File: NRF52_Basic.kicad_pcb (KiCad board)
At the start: 4 copper layers, 18.2 x 19.2 mm, 18 parts, among them J1 Conn_01x05_Male, J2 Conn_01x05_Male, J3 Conn_01x04_Male, J4 Conn_Coaxial, U1 nRF52832-QFxx, Y1 Crystal, Y2 Crystal

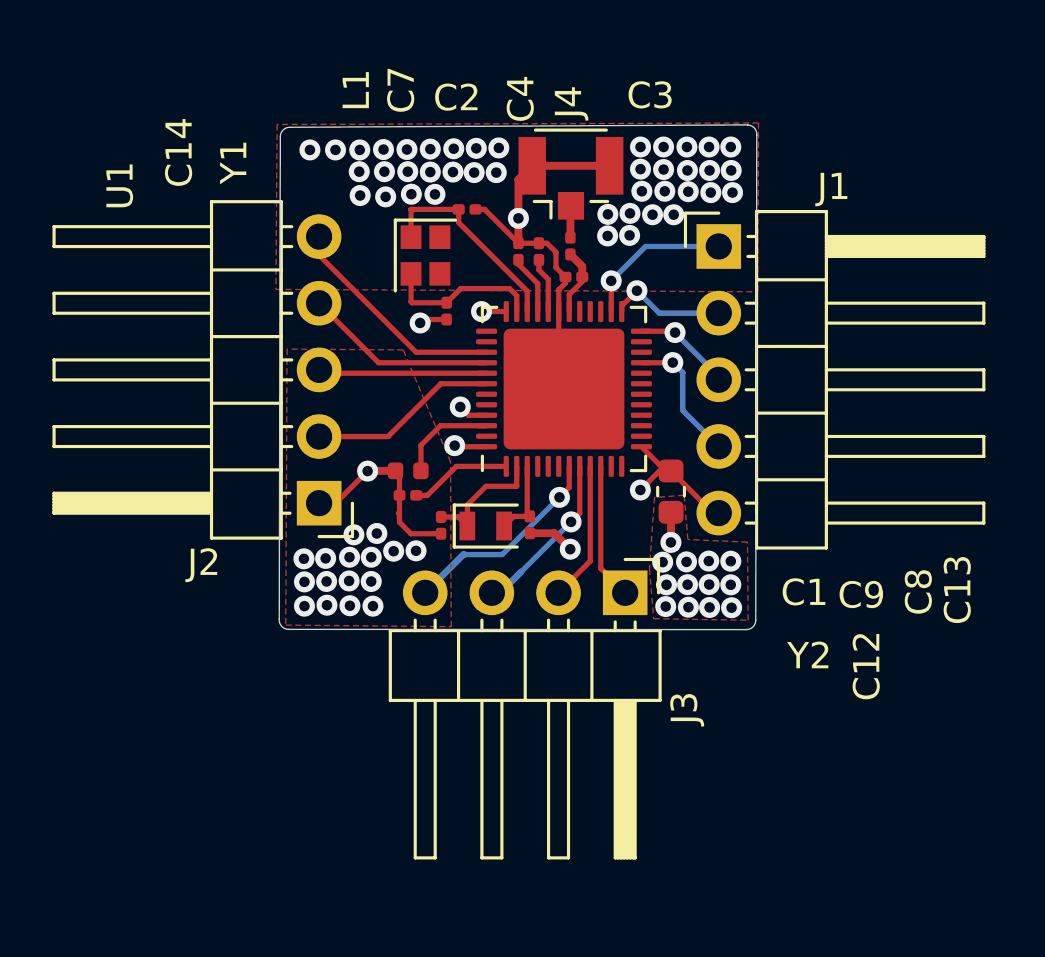
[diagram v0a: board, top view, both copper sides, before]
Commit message: Improved ground fills and structure
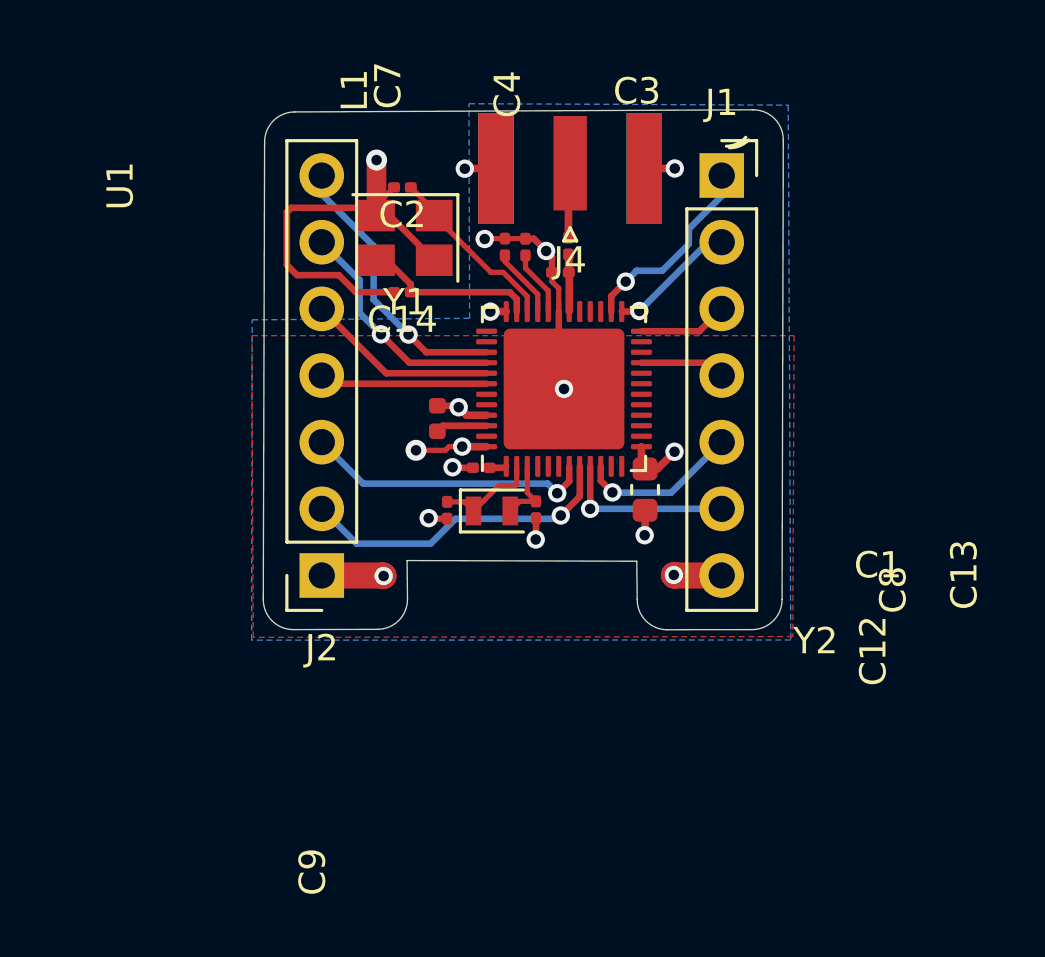
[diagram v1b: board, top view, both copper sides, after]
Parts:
- removed J3: Conn_01x04_Male, Connector_PinHeader_2.54mm:PinHeader_1x04_P2.54mm_Horizontal
- J1, J2: value Conn_01x05_Male -> Conn_01x07_Male; footprint Connector_PinHeader_2.54mm:PinHeader_1x05_P2.54mm_Horizontal -> Connector_PinSocket_2.54mm:PinSocket_1x07_P2.54mm_Vertical
- J4: footprint Connector_Coaxial:U.FL_Hirose_U.FL-R-SMT-1_Vertical -> Connector_Coaxial:SMA_Samtec_SMA-J-P-H-ST-EM1_EdgeMount
- Y1: value Crystal -> Crystal_GND24; footprint Crystal:Crystal_SMD_2016-4Pin_2.0x1.6mm -> Crystal:Crystal_SMD_3225-4Pin_3.2x2.5mm
- moved C1 2.99 mm to (143.2, 86.4)
- moved J2 2.76 mm to (137.1, 90.5)
- moved J1 2.70 mm to (152.4, 75.3)
- moved C2 2.60 mm to (140.2, 75.7), turned to 180 degrees
- moved C9 2.28 mm to (141.5, 84.5), turned to 270 degrees
- moved C14 1.83 mm to (140.2, 79.7), turned to 180 degrees
- moved Y1 1.02 mm to (140.3, 77.7), turned to 180 degrees
- moved C8 0.99 mm to (149.5, 87.3)
- moved C13 0.62 mm to (145.3, 88.0)
- moved C12 0.62 mm to (141.9, 88.0)
- moved Y2 0.62 mm to (143.6, 88.1)
- moved C3 0.54 mm to (146.2, 79.0)
- moved C4 0.54 mm to (144.9, 78.0)
- moved C7 0.54 mm to (144.1, 78.0)
- moved J4 0.37 mm to (146.6, 75.0)
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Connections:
- J1 pad 5: VDD -> 0.08_RX
- J2 pad 2: 0.30 -> 0.06_TX
- J2 pad 3: 0.29 -> 0.05_RTS
- J2 pad 4: 0.28 -> 0.30
- J2 pad 5: 0.27 -> 0.29
- Y1 pad 2: XC2 -> VSS
- Y1 pad 3: (no net) -> XC2
- Y1 pad 4: (no net) -> VSS
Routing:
- net VSS: track 27.8 -> 34.7 mm, vias 75 -> 12
- net 0.06_TX: track 7.46 -> 12.3 mm
- net D1: track 3.89 -> 0.66 mm
- net 0.05_RTS: track 7.96 -> 11.0 mm
- net 0.27: track 8.62 -> 10.7 mm, vias 0 -> 1
- net SWO: track 5.12 -> 3.26 mm, vias 1 -> 0
- net D4: track 3.78 -> 1.96 mm
- net Net-(J4-Pad1): track 1.22 -> 2.86 mm
- net SWDIO: track 5.81 -> 7.45 mm
- net 0.28: track 7.32 -> 8.92 mm, vias 0 -> 1
- net 0.07_CTS: track 5.32 -> 6.63 mm, vias 0 -> 1
- net XC1: track 7.85 -> 6.84 mm
- net XL1: track 4.88 -> 3.89 mm
- net 0.08_RX: track 5.20 -> 6.14 mm, vias 0 -> 1
- net 0.29: track 6.43 -> 7.30 mm
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- added copper zone on B.Cu, net VDD
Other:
- board size 18.2 x 19.2 mm -> 19.8 x 19.8 mm
- net class Default: clearance 0.2 -> 0.127
- net class GND removed
- net class VCC removed
- rule trace_clearance: 0.2 -> 0.127

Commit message: Intermediate mods -2
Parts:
- C1: value C -> 100nF
- C12, C13, C14, C2: value C -> 12pF
- C3: value C -> 0.8pF
- C4, C7: value C -> 100pF
- C8: value C -> 4.7uF
- C9: value C -> 1.0uF
- L1: value L -> 3.9nH
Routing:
- net VDD: track 7.49 -> 11.5 mm, vias 5 -> 8
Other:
- board text added: "0.05/RTS"
- board text added: "0.06/TX"
- board text added: "0.07/CTS"
- board text added: "0.08/RX"
- board text added: "0.27"
- board text added: "0.28"
- board text added: "0.29"
- board text added: "0.30"
- board text added: "GND"
- board text added: "NRF52 V1 J.S.I.A"
- board text added: "RESET/0.21"
- board text added: "SWDCLK"
- board text added: "SWDIO"
- board text added: "SWO"

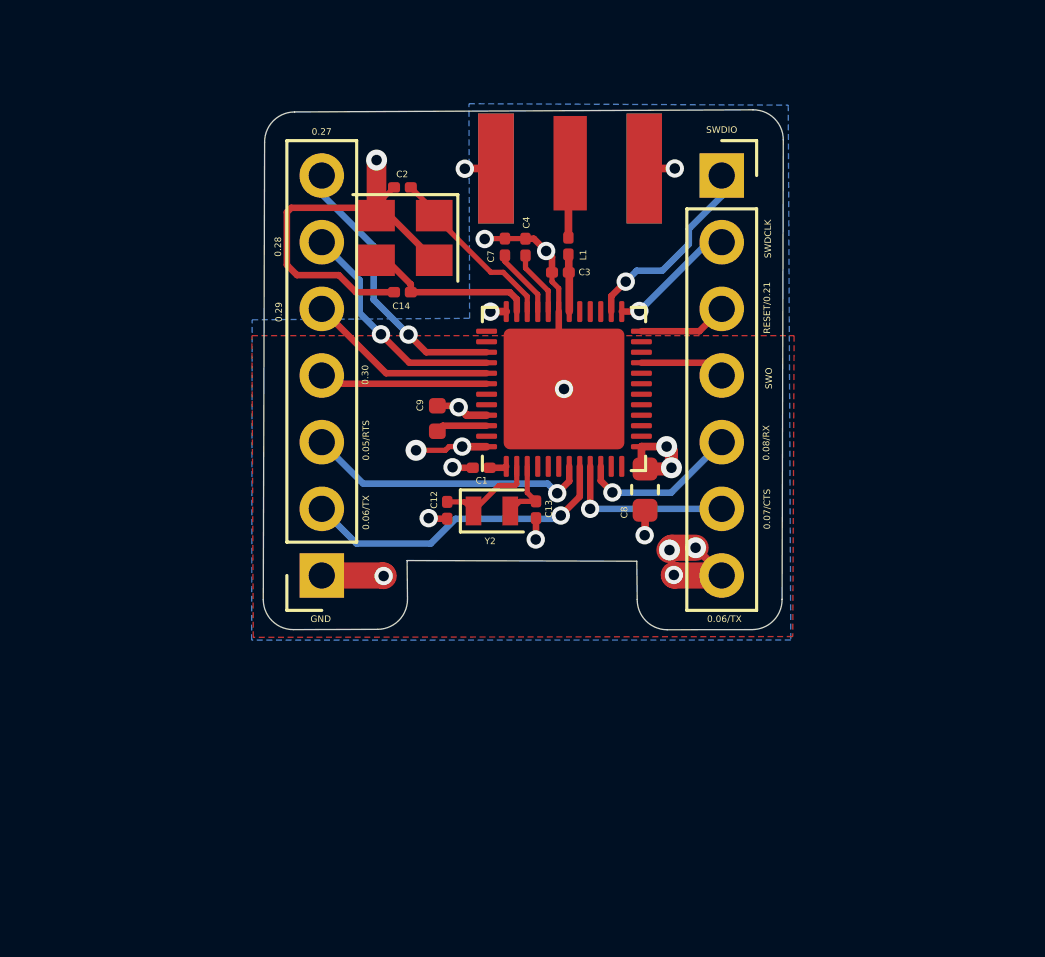
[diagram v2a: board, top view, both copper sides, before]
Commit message: Optimized the layers and component fixtures
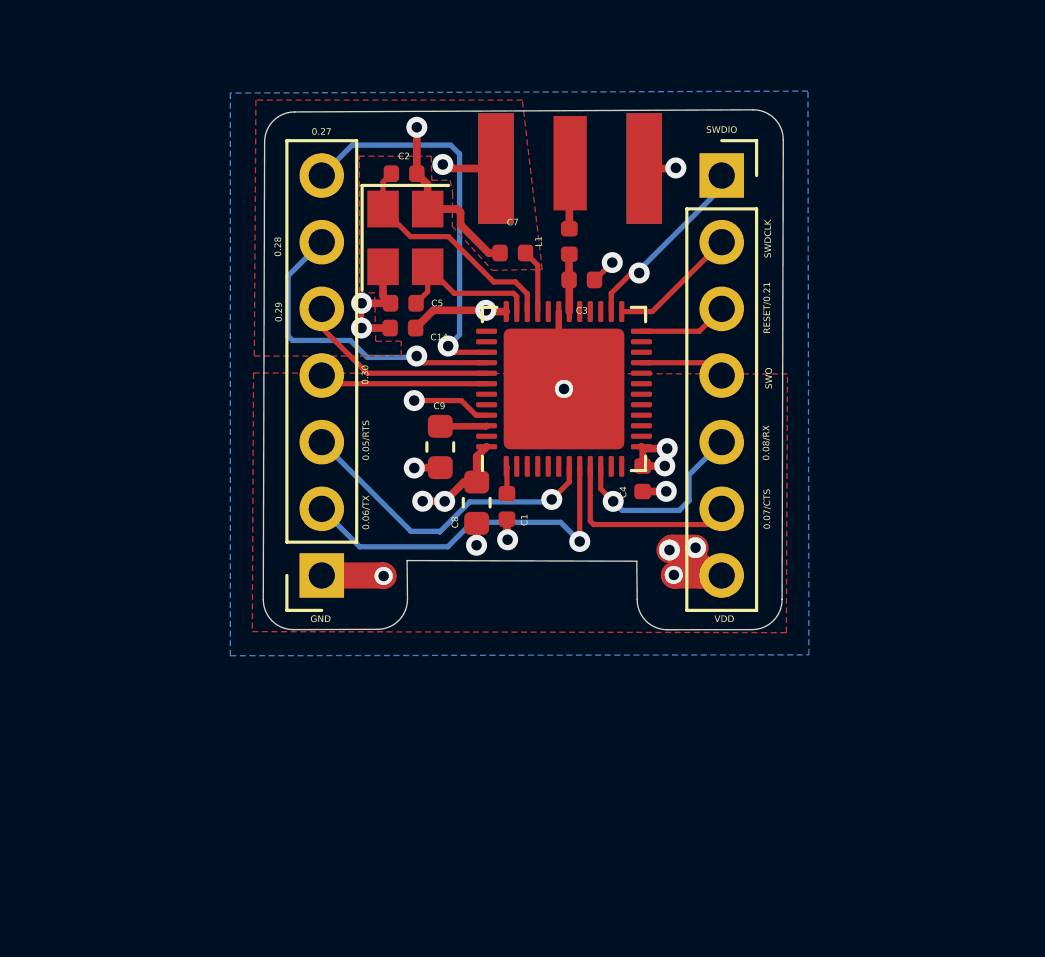
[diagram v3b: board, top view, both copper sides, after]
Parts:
- removed C12, C13: 12pF, Capacitor_SMD:C_0201_0603Metric
- removed Y2: Crystal, Crystal:Crystal_SMD_2012-2Pin_2.0x1.2mm
- added C5: 100nF, Capacitor_SMD:C_0402_1005Metric, F.Cu at (140.2, 81.1)
- C1, C14, C2, C3, C7: footprint Capacitor_SMD:C_0201_0603Metric -> Capacitor_SMD:C_0402_1005Metric
- C4: value 100pF -> 100nF; footprint Capacitor_SMD:C_0201_0603Metric -> Capacitor_SMD:C_0402_1005Metric
- C9: footprint Capacitor_SMD:C_0402_1005Metric -> Capacitor_SMD:C_0603_1608Metric
- L1: footprint Inductor_SMD:L_0201_0603Metric -> Inductor_SMD:L_0402_1005Metric
- moved C4 9.89 mm to (149.4, 86.8), turned to 90 degrees
- moved C8 6.44 mm to (143.0, 87.8)
- moved C1 1.77 mm to (144.2, 87.9), turned to 90 degrees
- moved C9 1.09 mm to (141.7, 85.6), turned to 90 degrees
- moved C3 0.86 mm to (147.0, 79.3), turned to 180 degrees
- moved C2 0.53 mm to (140.3, 75.2), turned to 0 degrees
- moved C14 0.42 mm to (140.2, 80.2)
- moved C7 0.38 mm to (144.4, 78.2), turned to 0 degrees
- moved L1 0.18 mm to (146.6, 77.8)
- turned Y1 to 270 degrees
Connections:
- C4 pad 2: D2 -> VDD
- U1 pad 2: XL1 -> Net-(U1-Pad2)
- U1 pad 3: XL2 -> Net-(U1-Pad3)
- U1 pad 32: D2 -> Net-(U1-Pad32)
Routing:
- net VDD: track 11.5 -> 28.9 mm
- net VSS: track 34.7 -> 27.8 mm, vias 12 -> 13
- net 0.27: track 10.7 -> 14.9 mm
- net XL1: track 3.89 -> 0.00 mm
- net 0.28: track 8.92 -> 12.1 mm
- net XL2: track 2.60 -> 0.00 mm
- net D2: track 2.49 -> 0.00 mm
- net XC1: track 6.84 -> 8.99 mm
- net 0.06_TX: track 12.3 -> 14.0 mm
- net 0.08_RX: track 6.14 -> 7.46 mm
- net 0.05_RTS: track 11.0 -> 12.2 mm
- net 0.07_CTS: track 6.63 -> 7.40 mm, vias 1 -> 0
- net XC2: track 6.61 -> 6.01 mm
- net SWDCLK: vias 1 -> 0
- added copper zone on B.Cu, net VSS
- removed copper zone on B.Cu, net VDD
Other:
- board text added: "VDD"
